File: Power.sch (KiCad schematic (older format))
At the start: 38 parts

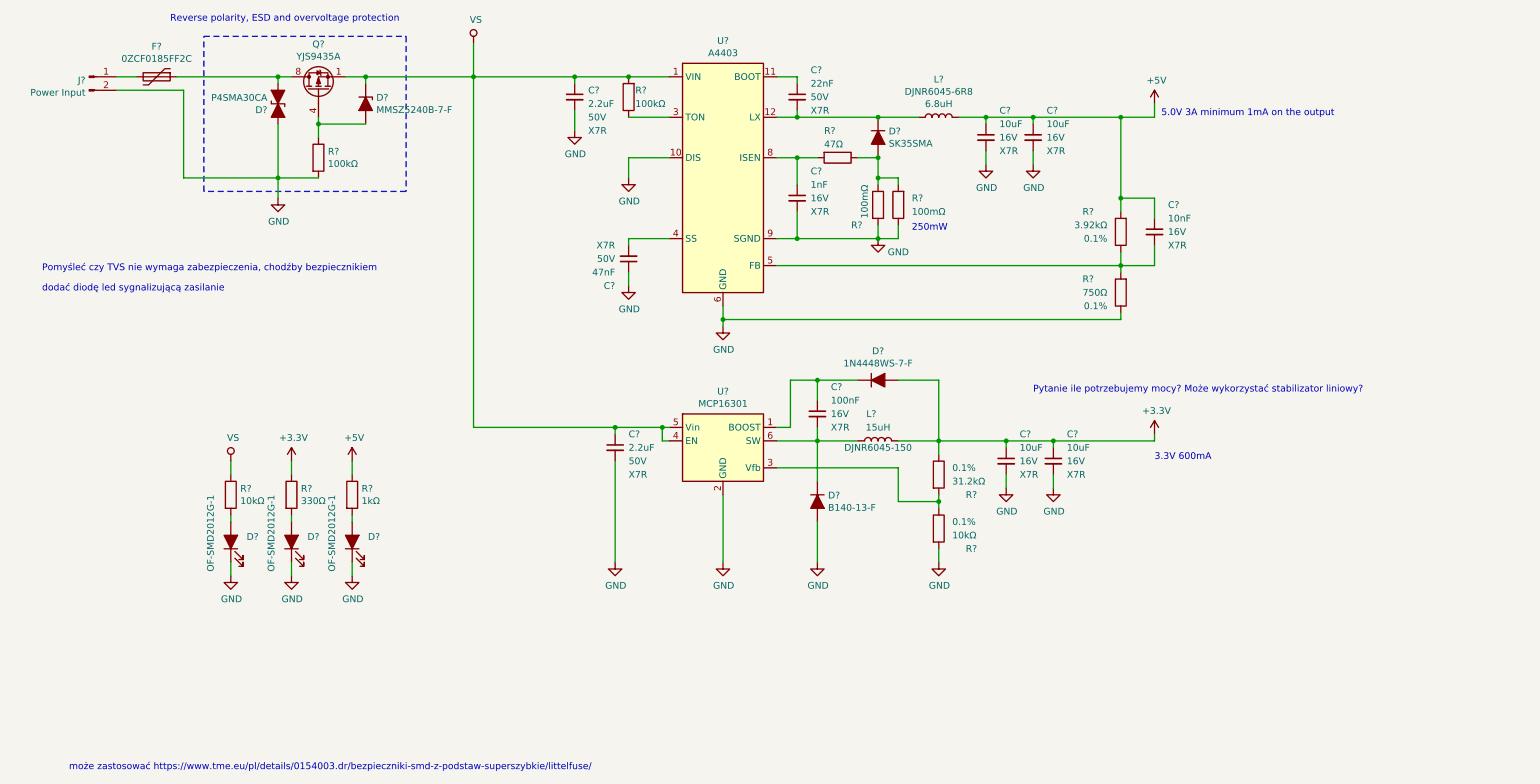
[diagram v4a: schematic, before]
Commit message: Numbering and finishing the schematic
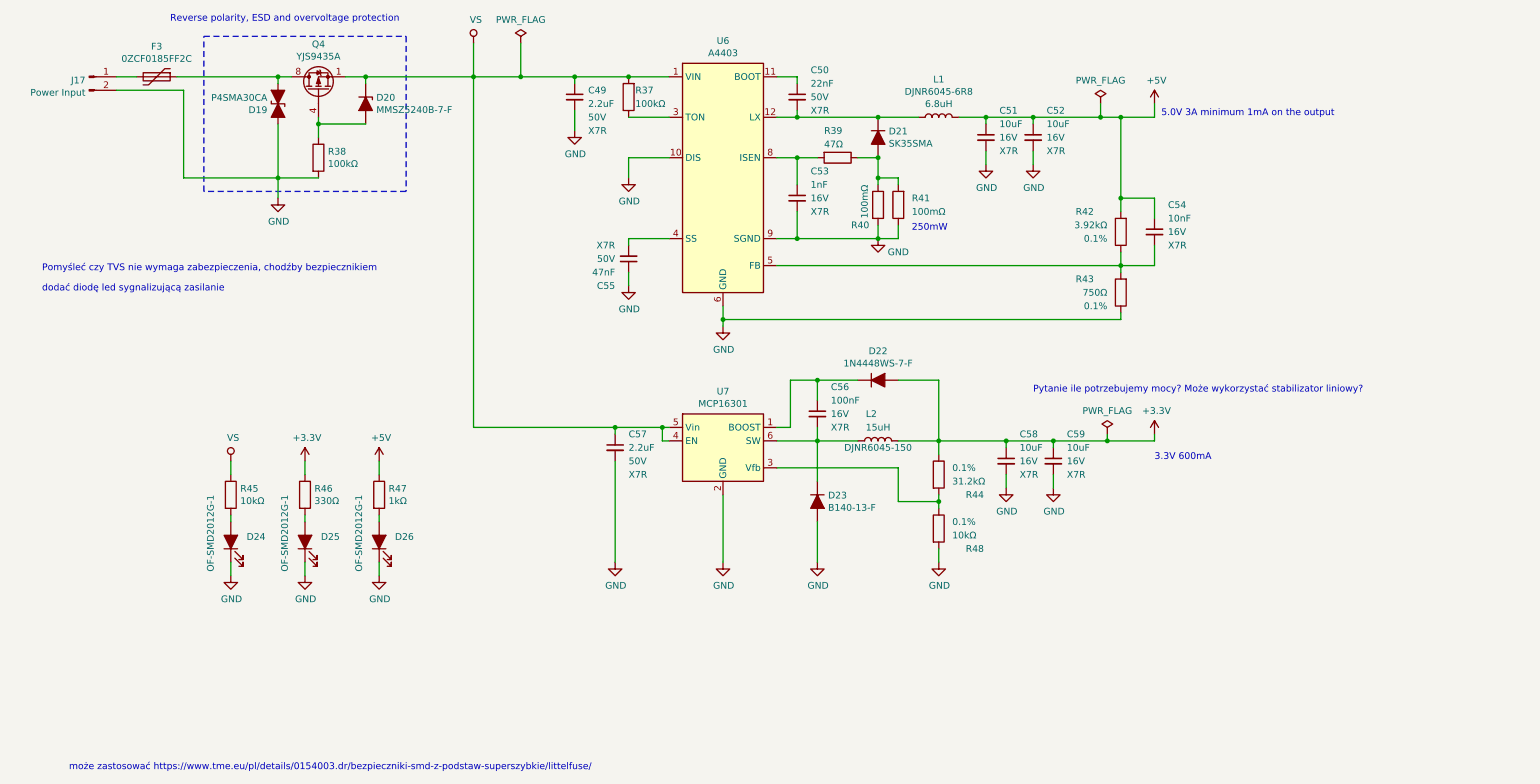
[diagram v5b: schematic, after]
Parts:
- L1, L2: renamed from L?; footprint (none) -> footprints:L_6.2x6.2_H4.5
- gave numbers to parts that had none: 36
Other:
- moved on the sheet: D25, D26, R46, R47

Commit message: Shematic almost finished, BOM in KiCad 3/4 finished
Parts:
- C49: footprint Capacitor_SMD:C_0603_1608Metric -> Capacitor_SMD:C_1206_3216Metric; Cena (none) -> 0.68179; Link (none) -> https://www.tme.eu/pl/details/cl31b225kbhnnne/kondensatory-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; Model (none) -> CL31B225KBHNNNE; Producent (none) -> SAMSUNG
- C50: renamed from C57; footprint (none) -> Capacitor_SMD:C_1206_3216Metric; Cena (none) -> 0.68179; Link (none) -> https://www.tme.eu/pl/details/cl31b225kbhnnne/kondensatory-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; Model (none) -> CL31B225KBHNNNE; Producent (none) -> SAMSUNG
- C52: renamed from C50; Cena (none) -> 0.07284; Link (none) -> https://www.tme.eu/pl/details/cc0603krx7r9223/kondensatory-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; Model (none) -> CC0603KRX7R9223; Producent (none) -> YAGEO; Tolerancja (none) -> 10%; Typ (none) -> SMD
- C54: renamed from C56; value 100nF -> 0.1uF; footprint (none) -> Capacitor_SMD:C_0603_1608Metric; Cena (none) -> 0.05982; Model (none) -> CL10B104KB8NNNC; Napięcie 16V -> 50V; Producent (none) -> SAMSUNG; Tolerancja (none) -> 10%; Typ (none) -> SMD
- C55: renamed from C51; footprint (none) -> Capacitor_SMD:C_1206_3216Metric; Cena (none) -> 0.26552; Model (none) -> CL31B106KAHNNNE; Producent (none) -> SAMSUNG; Tolerancja (none) -> 10%; Typ (none) -> SMD
- C56: renamed from C58; footprint (none) -> Capacitor_SMD:C_1206_3216Metric; Cena (none) -> 0.26552; Model (none) -> CL31B106KAHNNNE; Producent (none) -> SAMSUNG; Tolerancja (none) -> 10%; Typ (none) -> SMD
- C57: renamed from C52; footprint (none) -> Capacitor_SMD:C_1206_3216Metric; Cena (none) -> 0.26552; Model (none) -> CL31B106KAHNNNE; Producent (none) -> SAMSUNG; Tolerancja (none) -> 10%; Typ (none) -> SMD
- C58: renamed from C59; footprint (none) -> Capacitor_SMD:C_1206_3216Metric; Cena (none) -> 0.26552; Model (none) -> CL31B106KAHNNNE; Producent (none) -> SAMSUNG; Tolerancja (none) -> 10%; Typ (none) -> SMD
- D19: renamed from D24; Cena (none) -> 0.34; Link (none) -> https://www.tme.eu/pl/details/of-smd2012g-1/diody-led-smd-k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; Model (none) -> OF-SMD2012G-1; Opis (none) -> LED; SMD; 0805; zielony; 600÷800mcd; 2x1,25x0,68mm; 120°; 2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; Producent (none) -> OPTOFLASH; Typ (none) -> SMD
- D20: renamed from D19; Cena (none) -> 0.60763; Link (none) -> https://www.tme.eu/pl/details/p4sma30ca-yan/diody-transil-s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; Model (none) -> P4SMA30CA; Opis (none) -> Dioda: transil; 400W; 30V; 9,6A; dwukierunkowa; ±5%; Producent (none) -> YANGJIE TECHNOLOGY; Typ (none) -> SMD
- D21: renamed from D25; Cena (none) -> 0.34; Link (none) -> https://www.tme.eu/pl/details/of-smd2012g-1/diody-led-smd-k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; Model (none) -> OF-SMD2012G-1; Opis (none) -> LED; SMD; 0805; zielony; 600÷800mcd; 2x1,25x0,68mm; 120°; 2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; Producent (none) -> OPTOFLASH; Typ (none) -> SMD
- D22: renamed from D20; Cena (none) -> 0.10646; Link (none) -> https://www.tme.eu/pl/details/mmsz5240b-7-f/diody-zenera-sm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; Model (none) -> MMSZ5240B-7-F; Opis (none) -> Dioda: Zenera; 0,37/0,5W; 10V; SMD; rolka,taśma; SOD123; Producent (none) -> DIODES INCORPORATED; Typ (none) -> SMD
- D23: renamed from D26; Cena (none) -> 0.34; Link (none) -> https://www.tme.eu/pl/details/of-smd2012g-1/diody-led-smd-k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; Model (none) -> OF-SMD2012G-1; Opis (none) -> LED; SMD; 0805; zielony; 600÷800mcd; 2x1,25x0,68mm; 120°; 2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; Producent (none) -> OPTOFLASH; Typ (none) -> SMD
- D24: renamed from D23; footprint (none) -> Diode_SMD:D_SMA; Cena (none) -> 0.2938; Link (none) -> https://www.tme.eu/pl/details/b140-13-f/diody-schottky-smd/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; Model (none) -> B140-13-F; Opis (none) -> Dioda: prostownicza Schottky; SMD; 40V; 1A; SMA; Producent (none) -> DIODES INCORPORATED; Typ (none) -> SMD
- D25: renamed from D21; Cena (none) -> 0.3496; Link (none) -> https://www.tme.eu/pl/details/sk35sma-dio/diody-schottky-sm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; Model (none) -> SK35SMA; Opis (none) -> Dioda: prostownicza Schottky; SMD; 50V; 3A; SMA; Producent (none) -> DIODES INCORPORATED; Typ (none) -> SMD
- D26: renamed from D22; footprint (none) -> Diode_SMD:D_SOD-323; Cena (none) -> 0.14905; Link (none) -> https://www.tme.eu/pl/details/1n4448ws-7-f/diody-uniwersaln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; Model (none) -> 1N4448WS-7-F; Opis (none) -> Dioda: prostownicza; SMD; 75V; 0,25A; 4ns;; Producent (none) -> DIODES INCORPORATED; Typ (none) -> SMD
- F3: value 0ZCF0185FF2C -> 0ZCF0185FF2C; Cena (none) -> 0.8689; Link (none) -> https://www.tme.eu/pl/details/0zcf0185ff2c/bezpieczniki-pol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; Model (none) -> 0ZCF0185FF2C; Opis (none) -> Bezpiecznik: polimerowy PTC; 1,85A; Imax: 100A; Obud: 2920;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; Producent (none) -> BEL FUSE; Typ (none) -> SMD
- R38: renamed from R46; footprint (none) -> Resistor_SMD:R_0603_1608Metric
- R40: renamed from R47; footprint (none) -> Resistor_SMD:R_0603_1608Metric
- R41: renamed from R37; footprint (none) -> Resistor_SMD:R_0603_1608Metric
- U6: Cena (none) -> 6.66; Link (none) -> https://www.tme.eu/pl/details/a4403geutr-t/regulatory-napie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; Model (none) -> A4403GEUTR-T; Opis (none) -> PMIC; przetwornica DC/DC; Upracy: 9÷46V; Uwyj: 46V; QFN16; 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; Producent (none) -> ALLEGRO; Typ (none) -> SMD
- U7: Cena (none) -> 3.82; Link (none) -> https://www.tme.eu/pl/details/mcp16301t-i_chy/regulatory-na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; Model (none) -> MCP16301T-I/CHY; Opis (none) -> PMIC; przetwornica DC/DC; Upracy: 4÷30V; Uwyj: 2÷15V; SOT23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; Producent (none) -> MICROCHIP; Typ (none) -> SMD
- renumbered C55 to C51, C54 to C59, L2 to L1, L1 to L2, R45 to R37, R38 to R39, R39 to R42, R40 to R43, R41 to R44, R44 to R45, R48 to R46, R42 to R47, R43 to R48

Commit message: BOM in KiCad almost finished, genereated NETLIST, create PCB
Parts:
- C49, C50, C51, C59: Typ (none) -> SMD
- C53: Cena (none) -> 0.05563; Link (none) -> https://www.tme.eu/pl/details/cl10b102kb8nnnc/kondensatory-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; Model (none) -> CL10B102KB8NNNC; Opis (none) -> Kondensator: ceramiczny; MLCC; 1nF; 50V; X7R; ±10%; SMD; 06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; Producent (none) -> SAMSUNG; Typ (none) -> SMD
- J17: Cena (none) -> 0.49272; Link (none) -> https://www.tme.eu/pl/details/b2b-xh-a/zlacza-sygnalowe-ras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; Model (none) -> B2B-XH-A; Opis (none) -> Gniazdo; przewód-płytka; męskie; XH; 2,5mm; PIN: 2; THT; 25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; Producent (none) -> JST; Typ (none) -> THT
- L1: Cena (none) -> 0.7018; Link (none) -> https://www.tme.eu/pl/details/djnr6045-150/dlawiki-smd-mocy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; Model (none) -> DJNR6045-150; Opis (none) -> Dławik: drutowy; SMD; 15uH; Ipracy: 2,3A; 100,1mΩ; 6x5,9x4,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; Producent (none) -> FERROCORE; Typ (none) -> SMD
- L2: Cena (none) -> 0.7018; Link (none) -> https://www.tme.eu/pl/details/djnr6045-6r8/dlawiki-smd-mocy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; Model (none) -> DJNR6045-6R8; Opis (none) -> Dławik: drutowy; SMD; 6,8uH; Ipracy: 3,5A; 49,4mΩ; 6x5,9x4,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; Producent (none) -> FERROCORE; Typ (none) -> SMD
- Q4: Cena (none) -> 0.29736; Link (none) -> https://www.tme.eu/pl/details/yjs9435a-yan/tranzystory-z-ka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; Model (none) -> YJS9435A; Opis (none) -> Tranzystor: P-MOSFET; TRENCH POWER LV; unipolarny; -30V; -4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; Producent (none) -> YANGJIE TECHNOLOGY; Typ (none) -> SMD
- R37, R38, R39, R41, R42, R48: Cena (none) -> 0.04651; Typ (none) -> SMD
- R40: Cena (none) -> 0.04651; Link (none) -> https://www.tme.eu/pl/details/smd0603-1k-1%25/rezystory-smd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; Model (none) -> 0603SAF1001T5E; Opis (none) -> Rezystor: thick film; SMD; 0603; 1kΩ; 0,1W; ±1%; -55÷155°C; Producent (none) -> ROYAL OHM; Typ (none) -> SMD
- R43, R44: Cena (none) -> 0.33547; Link (none) -> https://www.tme.eu/pl/details/smd1206-r10-lo/rezystory-smd-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; Model (none) -> 6-1622825-5; Opis (none) -> Rezystor: metal glaze; SMD; 1206; 100mΩ; 0,25W; ±5%; 200ppm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; Producent (none) -> TE Connectivity; Typ (none) -> SMD
- R45: Cena (none) -> 0.02; Link (none) -> https://pl.farnell.com/multicomp/mcwr06x3162ftl/res-31k6-1-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; Model (none) -> MCWR06X3162FTL; Opis (none) -> Rezystor SMD, grubowarstwowy, 0603 [jedn. metryczne: 1608],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; Producent (none) -> MULTICOMP PRO; Typ (none) -> SMD
- R46: Cena (none) -> 0.03622; Link (none) -> https://www.tme.eu/pl/details/smd0603-10k-1%25/rezystory-sm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; Model (none) -> 0603SAF1002T5E; Opis (none) -> Rezystor: thick film; SMD; 0603; 10kΩ; 0,1W; ±1%; -55÷155°C; Producent (none) -> ROYAL OHM; Typ (none) -> SMD
- R47: Cena (none) -> 0.05158; Link (none) -> https://www.tme.eu/pl/details/smd0603-3.92k-1%25/rezystory-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; Model (none) -> 0603SAF3921T5E; Opis (none) -> Rezystor: thick film; SMD; 0603; 3,92kΩ; 0,1W; ±1%; -55÷155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; Producent (none) -> ROYAL OHM; Typ (none) -> SMD
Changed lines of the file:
@@
 F 3 "~" H 6550 2350 50  0001 C CNN
 F 4 "" H 6550 2350 50  0001 C CNN "Model"
+F 5 "0.04651" H 6550 2350 50  0001 C CNN "Cena"
+F 6 "SMD" H 6550 2350 50  0001 C CNN "Typ"
 	1    6550 2350
 	0    1    1    0
@@
 F 4 "16V" H 6350 2650 50  0000 L CNN "Napięcie"
 F 5 "X7R" H 6350 2550 50  0000 L CNN "Dielektryk"
+F 6 "0.05563" H 6250 2650 50  0001 C CNN "Cena"
+F 7 "https://www.tme.eu/pl/details/cl10b102kb8nnnc/kondensatory-mlcc-smd-0603/samsung/" H 6250 2650 50  0001 C CNN "Link"
+F 8 "CL10B102KB8NNNC" H 6250 2650 50  0001 C CNN "Model"
+F 9 "Kondensator: ceramiczny; MLCC; 1nF; 50V; X7R; ±10%; SMD; 0603" H 6250 2650 50  0001 C CNN "Opis"
+F 10 "SAMSUNG" H 6250 2650 50  0001 C CNN "Producent"
+F 11 "SMD" H 6250 2650 50  0001 C CNN "Typ"
 	1    6250 2650
 	1    0    0    -1
@@
 F 3 "~" H 7300 2050 50  0001 C CNN
 F 4 "6.8uH" V 7399 2050 50  0000 C CNN "Induktancja"
+F 5 "0.7018" H 7300 2050 50  0001 C CNN "Cena"
+F 6 "https://www.tme.eu/pl/details/djnr6045-6r8/dlawiki-smd-mocy/ferrocore/" H 7300 2050 50  0001 C CNN "Link"
+F 7 "DJNR6045-6R8" H 7300 2050 50  0001 C CNN "Model"
+F 8 "Dławik: drutowy; SMD; 6,8uH; Ipracy: 3,5A; 49,4mΩ; 6x5,9x4,5mm; ±20%" H 7300 2050 50  0001 C CNN "Opis"
+F 9 "FERROCORE" H 7300 2050 50  0001 C CNN "Producent"
+F 10 "SMD" H 7300 2050 50  0001 C CNN "Typ"
 	1    7300 2050
 	0    -1   -1   0
@@
 F 2 "Resistor_SMD:R_1206_3216Metric" V 6930 2700 50  0001 C CNN
 F 3 "~" H 7000 2700 50  0001 C CNN
-F 4 "" H 7000 2700 50  0001 C CNN "Model"
+F 4 "6-1622825-5" H 7000 2700 50  0001 C CNN "Model"
+F 5 "0.33547" H 7000 2700 50  0001 C CNN "Cena"
+F 6 "https://www.tme.eu/pl/details/smd1206-r10-lo/rezystory-smd-1206/te-connectivity/6-1622825-5/" H 7000 2700 50  0001 C CNN "Link"
+F 7 "Rezystor: metal glaze; SMD; 1206; 100mΩ; 0,25W; ±5%; 200ppm/°C" H 7000 2700 50  0001 C CNN "Opis"
+F 8 "TE Connectivity" H 7000 2700 50  0001 C CNN "Producent"
+F 9 "SMD" H 7000 2700 50  0001 C CNN "Typ"
 	1    7000 2700
 	-1   0    0    1
@@
 F 3 "~" H 8650 2900 50  0001 C CNN
 F 4 "0.1%" H 8750 2950 50  0000 L CNN "Tolerancja"
-F 5 "" H 8650 2900 50  0001 C CNN "Model"
+F 5 "0603SAF3921T5E" H 8650 2900 50  0001 C CNN "Model"
+F 6 "0.05158" H 8650 2900 50  0001 C CNN "Cena"
+F 7 "https://www.tme.eu/pl/details/smd0603-3.92k-1%25/rezystory-smd-0603/royal-ohm/0603saf3921t5e/" H 8650 2900 50  0001 C CNN "Link"
+F 8 "Rezystor: thick film; SMD; 0603; 3,92kΩ; 0,1W; ±1%; -55÷155°C" H 8650 2900 50  0001 C CNN "Opis"
+F 9 "ROYAL OHM" H 8650 2900 50  0001 C CNN "Producent"
+F 10 "SMD" H 8650 2900 50  0001 C CNN "Typ"
 	1    8650 2900
 	-1   0    0    1
@@
 F 4 "16V" H 9000 2900 50  0000 L CNN "Napięcie"
 F 5 "X7R" H 9000 2800 50  0000 L CNN "Dielektryk"
+F 6 "SMD" H 8900 2900 50  0001 C CNN "Typ"
 	1    8900 2900
 	1    0    0    -1
@@
 F 4 "0.1%" H 8750 3450 50  0000 L CNN "Tolerancja"
 F 5 "" H 8650 3350 50  0001 C CNN "Model"
+F 6 "0.04651" H 8650 3350 50  0001 C CNN "Cena"
+F 7 "SMD" H 8650 3350 50  0001 C CNN "Typ"
 	1    8650 3350
 	-1   0    0    1
@@
 F 4 "50V" H 5100 3100 50  0000 L CNN "Napięcie"
 F 5 "X7R" H 5100 3000 50  0000 L CNN "Dielektryk"
+F 6 "SMD" H 5000 3100 50  0001 C CNN "Typ"
 	1    5000 3100
 	-1   0    0    1
@@
 F 3 "~" H 5000 1900 50  0001 C CNN
 F 4 "" H 5000 1900 50  0001 C CNN "Model"
+F 5 "0.04651" H 5000 1900 50  0001 C CNN "Cena"
+F 6 "SMD" H 5000 1900 50  0001 C CNN "Typ"
 	1    5000 1900
 	-1   0    0    1
@@
 F 8 "CL31B225KBHNNNE" H 4600 1900 50  0001 C CNN "Model"
 F 9 "SAMSUNG" H 4600 1900 50  0001 C CNN "Producent"
+F 10 "SMD" H 4600 1900 50  0001 C CNN "Typ"
 	1    4600 1900
 	1    0    0    -1
@@
 F 8 "CL31B225KBHNNNE" H 4900 4500 50  0001 C CNN "Model"
 F 9 "SAMSUNG" H 4900 4500 50  0001 C CNN "Producent"
+F 10 "SMD" H 4900 4500 50  0001 C CNN "Typ"
 	1    4900 4500
 	1    0    0    -1
@@
 F 3 "~" H 6850 4450 50  0001 C CNN
 F 4 "15uH" V 6950 4450 50  0000 C CNN "Induktancja"
+F 5 "0.7018" H 6850 4450 50  0001 C CNN "Cena"
+F 6 "https://www.tme.eu/pl/details/djnr6045-150/dlawiki-smd-mocy/ferrocore/" H 6850 4450 50  0001 C CNN "Link"
+F 7 "DJNR6045-150" H 6850 4450 50  0001 C CNN "Model"
+F 8 "Dławik: drutowy; SMD; 15uH; Ipracy: 2,3A; 100,1mΩ; 6x5,9x4,5mm; ±20%" H 6850 4450 50  0001 C CNN "Opis"
+F 9 "FERROCORE" H 6850 4450 50  0001 C CNN "Producent"
+F 10 "SMD" H 6850 4450 50  0001 C CNN "Typ"
 	1    6850 4450
 	0    -1   -1   0
@@
 F 3 "~" H 7300 4700 50  0001 C CNN
 F 4 "0.1%" H 7400 4750 50  0000 L CNN "Tolerancja"
-F 5 "" H 7300 4700 50  0001 C CNN "Model"
+F 5 "MCWR06X3162FTL" H 7300 4700 50  0001 C CNN "Model"
+F 6 "SMD" H 7300 4700 50  0001 C CNN "Typ"
+F 7 "0.02" H 7300 4700 50  0001 C CNN "Cena"
+F 8 "https://pl.farnell.com/multicomp/mcwr06x3162ftl/res-31k6-1-0-1w-thick-film/dp/2447337RL" H 7300 4700 50  0001 C CNN "Link"
+F 9 "Rezystor SMD, grubowarstwowy, 0603 [jedn. metryczne: 1608], 31.6 kohm, Seria MCWR, 75 V" H 7300 4700 50  0001 C CNN "Opis"
+F 10 "MULTICOMP PRO" H 7300 4700 50  0001 C CNN "Producent"
 	1    7300 4700
 	1    0    0    -1
@@
 F 3 "~" H 7300 5100 50  0001 C CNN
 F 4 "0.1%" H 7400 5150 50  0000 L CNN "Tolerancja"
-F 5 "" H 7300 5100 50  0001 C CNN "Model"
+F 5 "0603SAF1002T5E" H 7300 5100 50  0001 C CNN "Model"
+F 6 "0.03622" H 7300 5100 50  0001 C CNN "Cena"
+F 7 "https://www.tme.eu/pl/details/smd0603-10k-1%25/rezystory-smd-0603/royal-ohm/0603saf1002t5e/" H 7300 5100 50  0001 C CNN "Link"
+F 8 "Rezystor: thick film; SMD; 0603; 10kΩ; 0,1W; ±1%; -55÷155°C" H 7300 5100 50  0001 C CNN "Opis"
+F 9 "ROYAL OHM" H 7300 5100 50  0001 C CNN "Producent"
+F 10 "SMD" H 7300 5100 50  0001 C CNN "Typ"
 	1    7300 5100
 	1    0    0    -1
@@
 F 2 "Resistor_SMD:R_1206_3216Metric" V 6780 2700 50  0001 C CNN
 F 3 "~" H 6850 2700 50  0001 C CNN
-F 4 "" H 6850 2700 50  0001 C CNN "Model"
+F 4 "6-1622825-5" H 6850 2700 50  0001 C CNN "Model"
+F 5 "0.33547" H 6850 2700 50  0001 C CNN "Cena"
+F 6 "https://www.tme.eu/pl/details/smd1206-r10-lo/rezystory-smd-1206/te-connectivity/6-1622825-5/" H 6850 2700 50  0001 C CNN "Link"
+F 7 "Rezystor: metal glaze; SMD; 1206; 100mΩ; 0,25W; ±5%; 200ppm/°C" H 6850 2700 50  0001 C CNN "Opis"
+F 8 "TE Connectivity" H 6850 2700 50  0001 C CNN "Producent"
+F 9 "SMD" H 6850 2700 50  0001 C CNN "Typ"
 	1    6850 2700
 	1    0    0    -1
@@
 F 2 "Connector_JST:JST_XH_B2B-XH-AM_1x02_P2.50mm_Vertical" H 1000 1750 50  0001 C CNN
 F 3 "~" H 1000 1750 50  0001 C CNN
+F 4 "0.49272" H 1000 1750 50  0001 C CNN "Cena"
+F 5 "https://www.tme.eu/pl/details/b2b-xh-a/zlacza-sygnalowe-raster-2-50mm/jst/" H 1000 1750 50  0001 C CNN "Link"
+F 6 "B2B-XH-A" H 1000 1750 50  0001 C CNN "Model"
+F 7 "Gniazdo; przewód-płytka; męskie; XH; 2,5mm; PIN: 2; THT; 250V; 3A" H 1000 1750 50  0001 C CNN "Opis"
+F 8 "JST" H 1000 1750 50  0001 C CNN "Producent"
+F 9 "THT" H 1000 1750 50  0001 C CNN "Typ"
 	1    1000 1750
 	1    0    0    -1
@@
 F 2 "Package_SO:SOP-8_3.9x4.9mm_P1.27mm" H 2900 1775 50  0001 L CIN
 F 3 "http://www.irf.com/product-info/datasheets/data/irf7606pbf.pdf" V 2700 1850 50  0001 L CNN
+F 4 "0.29736" H 2700 1850 50  0001 C CNN "Cena"
+F 5 "https://www.tme.eu/pl/details/yjs9435a-yan/tranzystory-z-kanalem-p-smd/yangjie-technology/yjs9435a/" H 2700 1850 50  0001 C CNN "Link"
+F 6 "YJS9435A" H 2700 1850 50  0001 C CNN "Model"
+F 7 "Tranzystor: P-MOSFET; TRENCH POWER LV; unipolarny; -30V; -4,1A" H 2700 1850 50  0001 C CNN "Opis"
+F 8 "YANGJIE TECHNOLOGY" H 2700 1850 50  0001 C CNN "Producent"
+F 9 "SMD" H 2700 1850 50  0001 C CNN "Typ"
 	1    2700 1850
 	0    -1   -1   0
@@
 F 2 "Resistor_SMD:R_0603_1608Metric" V 2630 2350 50  0001 C CNN
 F 3 "~" H 2700 2350 50  0001 C CNN
+F 4 "0.04651" H 2700 2350 50  0001 C CNN "Cena"
+F 5 "SMD" H 2700 2350 50  0001 C CNN "Typ"
 	1    2700 2350
 	1    0    0    -1
@@
 F 2 "Resistor_SMD:R_0603_1608Metric" V 2530 4850 50  0001 C CNN
 F 3 "~" H 2600 4850 50  0001 C CNN
+F 4 "0.04651" H 2600 4850 50  0001 C CNN "Cena"
+F 5 "SMD" H 2600 4850 50  0001 C CNN "Typ"
 	1    2600 4850
 	1    0    0    -1
@@
 F 2 "Resistor_SMD:R_0603_1608Metric" V 3080 4850 50  0001 C CNN
 F 3 "~" H 3150 4850 50  0001 C CNN
+F 4 "0.04651" H 3150 4850 50  0001 C CNN "Cena"
+F 5 "https://www.tme.eu/pl/details/smd0603-1k-1%25/rezystory-smd-0603/royal-ohm/0603saf1001t5e/" H 3150 4850 50  0001 C CNN "Link"
+F 6 "0603SAF1001T5E" H 3150 4850 50  0001 C CNN "Model"
+F 7 "Rezystor: thick film; SMD; 0603; 1kΩ; 0,1W; ±1%; -55÷155°C" H 3150 4850 50  0001 C CNN "Opis"
+F 8 "ROYAL OHM" H 3150 4850 50  0001 C CNN "Producent"
+F 9 "SMD" H 3150 4850 50  0001 C CNN "Typ"
 	1    3150 4850
 	1    0    0    -1
@@
 F 2 "Resistor_SMD:R_0805_2012Metric" V 1980 4850 50  0001 C CNN
 F 3 "~" H 2050 4850 50  0001 C CNN
+F 4 "0.04651" H 2050 4850 50  0001 C CNN "Cena"
+F 5 "SMD" H 2050 4850 50  0001 C CNN "Typ"
 	1    2050 4850
 	1    0    0    -1
